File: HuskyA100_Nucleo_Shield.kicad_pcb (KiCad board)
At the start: 2 copper layers, 58.4 x 99.1 mm, 21 parts, among them CN10 HEADER_17x2, CN7 HEADER_10x2, CN8 HEADER_8x2, CN9 HEADER_15x2, J1 Conn_01x03, J2 Conn_01x03, J3 Conn_01x04, J4 Conn_01x04

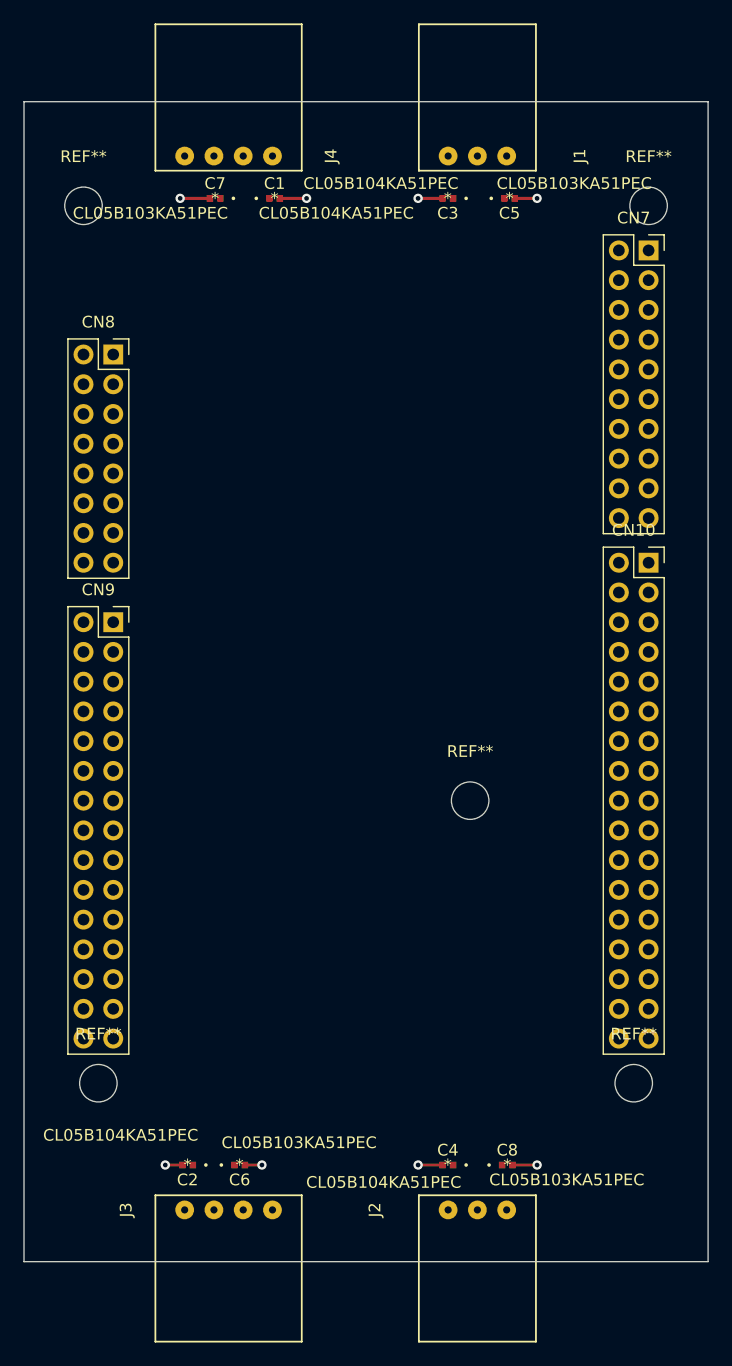
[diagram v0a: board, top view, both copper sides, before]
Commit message: routed the traces
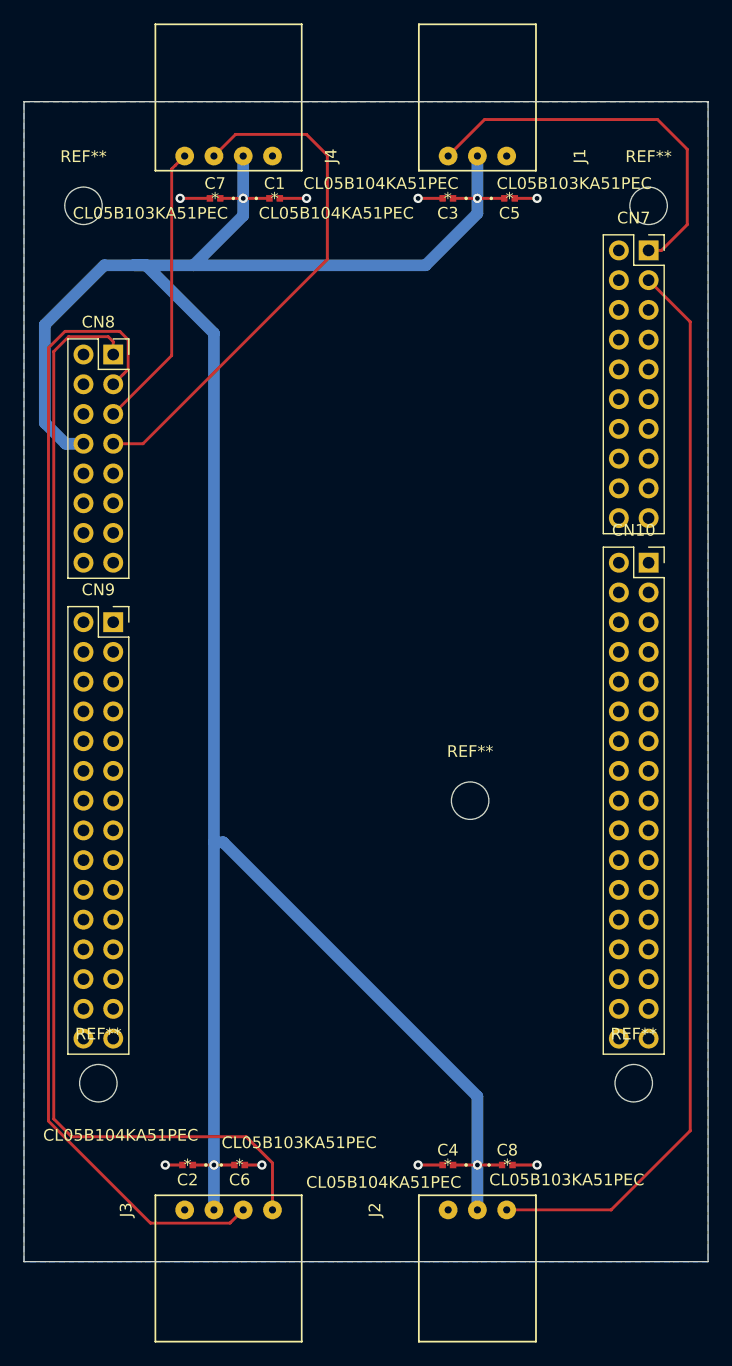
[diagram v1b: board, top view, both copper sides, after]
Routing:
- net 3.3V: track 0.00 -> 210.9 mm, vias 0 -> 4
- net Net-(CN8-Pad3): track 0.00 -> 98.7 mm
- net Net-(CN8-Pad1): track 0.00 -> 96.7 mm
- net Net-(CN7-Pad3): track 0.00 -> 92.6 mm
- net Net-(CN8-Pad7): track 0.00 -> 44.9 mm
- net Net-(CN7-Pad1): track 0.00 -> 33.4 mm
- net Net-(CN8-Pad5): track 0.00 -> 24.6 mm
- added copper zone on B.Cu, net GND
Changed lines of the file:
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@@
     (thickness 1.6)
     (drawings 4)
-    (tracks 16)
+    (tracks 90)
     (zones 0)
     (modules 21)
@@
   (segment (start 125.095 113.665) (end 122.9995 113.665) (width 0.25) (layer F.Cu) (net 7))
   (segment (start 117.0305 113.665) (end 114.935 113.665) (width 0.25) (layer F.Cu) (net 7))
+  (segment (start 135.72 35.56) (end 137.922 33.358) (width 0.25) (layer F.Cu) (net 8))
+  (segment (start 134.62 35.56) (end 135.72 35.56) (width 0.25) (layer F.Cu) (net 8))
+  (segment (start 137.922 33.358) (end 137.922 26.924) (width 0.25) (layer F.Cu) (net 8))
+  (segment (start 137.922 26.924) (end 135.382 24.384) (width 0.25) (layer F.Cu) (net 8))
+  (segment (start 120.616 24.384) (end 117.5 27.5) (width 0.25) (layer F.Cu) (net 8))
+  (segment (start 135.382 24.384) (end 120.616 24.384) (width 0.25) (layer F.Cu) (net 8))
+  (segment (start 138.176 41.656) (end 138.176 110.744) (width 0.25) (layer F.Cu) (net 9))
+  (segment (start 134.62 38.1) (end 138.176 41.656) (width 0.25) (layer F.Cu) (net 9))
+  (segment (start 131.42 117.5) (end 122.5 117.5) (width 0.25) (layer F.Cu) (net 9))
+  (segment (start 138.176 110.744) (end 131.42 117.5) (width 0.25) (layer F.Cu) (net 9))
+  (segment (start 88.9 43.35) (end 88.476 42.926) (width 0.25) (layer F.Cu) (net 26))
+  (segment (start 88.9 44.45) (end 88.9 43.35) (width 0.25) (layer F.Cu) (net 26))
+  (segment (start 88.476 42.926) (end 85.09 42.926) (width 0.25) (layer F.Cu) (net 26))
+  (segment (start 85.09 42.926) (end 83.82 44.196) (width 0.25) (layer F.Cu) (net 26))
+  (segment (start 83.82 44.196) (end 83.82 109.728) (width 0.25) (layer F.Cu) (net 26))
+  (segment (start 83.82 109.728) (end 85.344 111.252) (width 0.25) (layer F.Cu) (net 26))
+  (segment (start 102.5 116.36863) (end 102.5 117.5) (width 0.25) (layer F.Cu) (net 26))
+  (segment (start 100.260002 111.252) (end 102.5 113.491998) (width 0.25) (layer F.Cu) (net 26))
+  (segment (start 102.5 113.491998) (end 102.5 116.36863) (width 0.25) (layer F.Cu) (net 26))
+  (segment (start 85.344 111.252) (end 100.260002 111.252) (width 0.25) (layer F.Cu) (net 26))
+  (segment (start 83.36999 109.9144) (end 83.36999 43.88401) (width 0.25) (layer F.Cu) (net 27))
+  (segment (start 92.080591 118.625001) (end 83.36999 109.9144) (width 0.25) (layer F.Cu) (net 27))
+  (segment (start 98.874999 118.625001) (end 92.080591 118.625001) (width 0.25) (layer F.Cu) (net 27))
+  (segment (start 100 117.5) (end 98.874999 118.625001) (width 0.25) (layer F.Cu) (net 27))
+  (segment (start 84.77801 42.47599) (end 89.46599 42.47599) (width 0.25) (layer F.Cu) (net 27))
+  (segment (start 83.36999 43.88401) (end 84.77801 42.47599) (width 0.25) (layer F.Cu) (net 27))
+  (segment (start 90.17 45.72) (end 89.749999 46.140001) (width 0.25) (layer F.Cu) (net 27))
+  (segment (start 89.749999 46.140001) (end 88.9 46.99) (width 0.25) (layer F.Cu) (net 27))
+  (segment (start 90.17 43.18) (end 90.17 45.72) (width 0.25) (layer F.Cu) (net 27))
+  (segment (start 89.46599 42.47599) (end 90.17 43.18) (width 0.25) (layer F.Cu) (net 27))
+  (segment (start 94.200001 28.299999) (end 95 27.5) (width 0.25) (layer F.Cu) (net 28))
+  (segment (start 93.889999 28.610001) (end 94.200001 28.299999) (width 0.25) (layer F.Cu) (net 28))
+  (segment (start 93.889999 44.540001) (end 93.889999 28.610001) (width 0.25) (layer F.Cu) (net 28))
+  (segment (start 88.9 49.53) (end 93.889999 44.540001) (width 0.25) (layer F.Cu) (net 28))
+  (segment (start 86.36 52.07) (end 84.836 52.07) (width 1) (layer B.Cu) (net 29))
+  (segment (start 84.836 52.07) (end 83.058 50.292) (width 1) (layer B.Cu) (net 29))
+  (segment (start 83.058 50.292) (end 83.058 41.91) (width 1) (layer B.Cu) (net 29))
+  (segment (start 83.058 41.91) (end 88.138 36.83) (width 1) (layer B.Cu) (net 29))
+  (segment (start 100 32.588) (end 100 31.115) (width 1) (layer B.Cu) (net 29))
+  (segment (start 95.758 36.83) (end 100 32.588) (width 1) (layer B.Cu) (net 29))
+  (segment (start 95.758 36.83) (end 115.57 36.83) (width 1) (layer B.Cu) (net 29))
+  (segment (start 120 32.4) (end 120 31.115) (width 1) (layer B.Cu) (net 29))
+  (segment (start 115.57 36.83) (end 120 32.4) (width 1) (layer B.Cu) (net 29))
+  (segment (start 90.678 36.83) (end 91.694 36.83) (width 1) (layer B.Cu) (net 29))
+  (segment (start 88.138 36.83) (end 90.678 36.83) (width 1) (layer B.Cu) (net 29))
+  (segment (start 90.678 36.83) (end 95.758 36.83) (width 1) (layer B.Cu) (net 29))
+  (segment (start 91.694 36.83) (end 97.5 42.636) (width 1) (layer B.Cu) (net 29))
+  (segment (start 97.5 86.106) (end 98.298 86.106) (width 1) (layer B.Cu) (net 29))
+  (segment (start 97.5 42.636) (end 97.5 86.106) (width 1) (layer B.Cu) (net 29))
+  (segment (start 97.5 86.106) (end 97.5 113.665) (width 1) (layer B.Cu) (net 29))
+  (segment (start 120 107.808) (end 120 113.665) (width 1) (layer B.Cu) (net 29))
+  (segment (start 98.298 86.106) (end 120 107.808) (width 1) (layer B.Cu) (net 29))
+  (segment (start 100 31.115) (end 100 27.5) (width 1) (layer B.Cu) (net 29))
+  (via (at 100 31.115) (size 0.8) (drill 0.4) (layers F.Cu B.Cu) (net 29))
+  (segment (start 120 31.115) (end 120 27.5) (width 1) (layer B.Cu) (net 29))
+  (via (at 120 31.115) (size 0.8) (drill 0.4) (layers F.Cu B.Cu) (net 29))
+  (segment (start 97.5 113.665) (end 97.5 117.5) (width 1) (layer B.Cu) (net 29))
+  (via (at 97.5 113.665) (size 0.8) (drill 0.4) (layers F.Cu B.Cu) (net 29))
+  (segment (start 120 113.665) (end 120 117.5) (width 1) (layer B.Cu) (net 29))
+  (via (at 120 113.665) (size 0.8) (drill 0.4) (layers F.Cu B.Cu) (net 29))
+  (segment (start 117.9195 113.665) (end 120 113.665) (width 0.25) (layer F.Cu) (net 29))
+  (segment (start 122.1105 113.665) (end 120 113.665) (width 0.25) (layer F.Cu) (net 29))
+  (segment (start 99.2505 113.665) (end 97.5 113.665) (width 0.25) (layer F.Cu) (net 29))
+  (segment (start 95.6945 113.665) (end 97.5 113.665) (width 0.25) (layer F.Cu) (net 29))
+  (segment (start 98.044 31.115) (end 100 31.115) (width 0.25) (layer F.Cu) (net 29))
+  (segment (start 102.235 31.115) (end 100 31.115) (width 0.25) (layer F.Cu) (net 29))
+  (segment (start 117.9195 31.115) (end 120 31.115) (width 0.25) (layer F.Cu) (net 29))
+  (segment (start 122.301 31.115) (end 120 31.115) (width 0.25) (layer F.Cu) (net 29))
+  (segment (start 88.9 52.07) (end 91.44 52.07) (width 0.25) (layer F.Cu) (net 95))
+  (segment (start 91.44 52.07) (end 107.188 36.322) (width 0.25) (layer F.Cu) (net 95))
+  (segment (start 107.188 36.322) (end 107.188 27.432) (width 0.25) (layer F.Cu) (net 95))
+  (segment (start 107.188 27.432) (end 105.41 25.654) (width 0.25) (layer F.Cu) (net 95))
+  (segment (start 99.346 25.654) (end 97.5 27.5) (width 0.25) (layer F.Cu) (net 95))
+  (segment (start 105.41 25.654) (end 99.346 25.654) (width 0.25) (layer F.Cu) (net 95))
+  (zone (net 7) (net_name GND) (layer B.Cu) (hatch edge 0.508)
+    (connect_pads (clearance 0.508))
+    (min_thickness 0.254)
+    (fill yes (arc_segments 16) (thermal_gap 0.508) (thermal_bridge_width 0.508))
+    (polygon
+      (pts
+        (xy 81.28 22.86) (xy 139.7 22.86) (xy 139.7 121.92) (xy 81.28 121.92)
+      )
+    )
+  )
 )

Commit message: Fixed #3 - replaced bypass caps with 5.6mm x 5.0mm case size to make them more easiy solderable
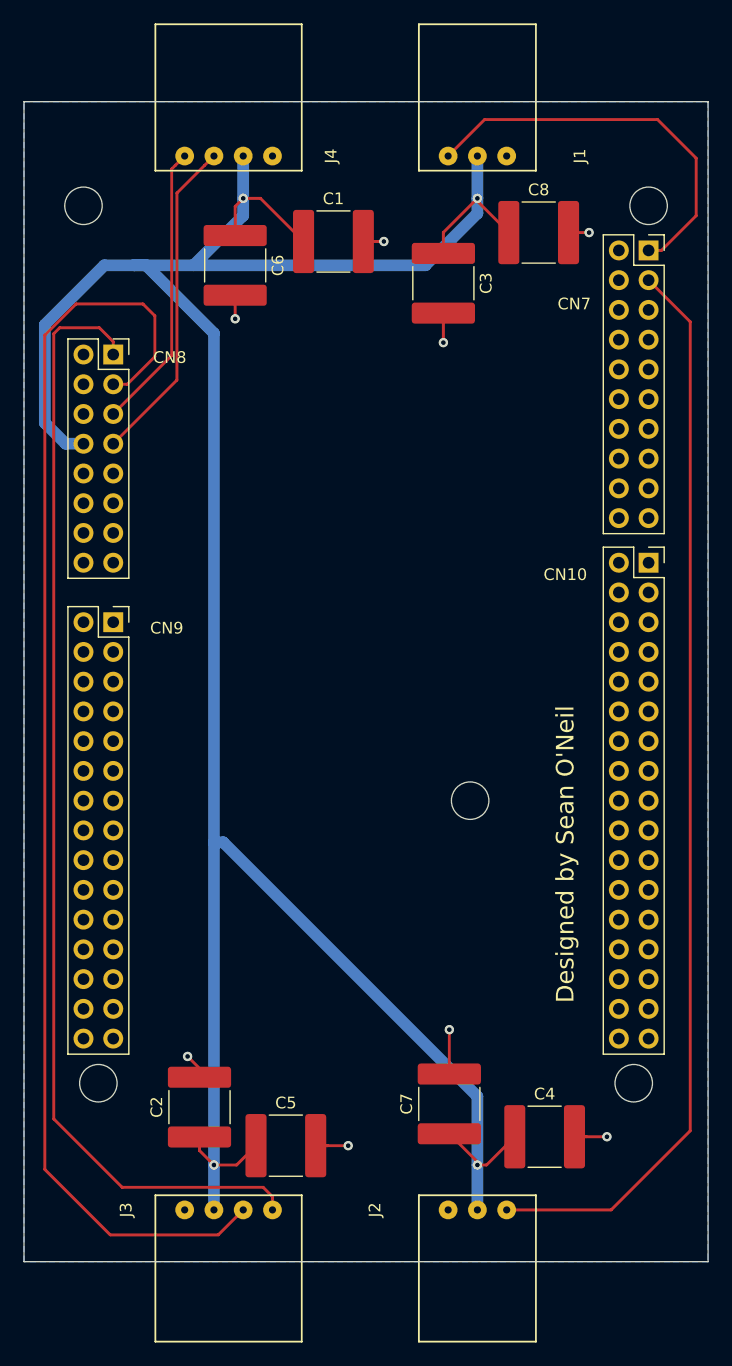
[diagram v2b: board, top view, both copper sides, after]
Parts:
- C1, C2, C3, C4: value CL05B104KA51PEC -> 0.01uF; footprint CL05B104KA51PEC -> Capacitor_SMD:C_2220_5650Metric
- C5, C6, C7, C8: value CL05B103KA51PEC -> 0.1uF; footprint CL05B103KA51PEC -> Capacitor_SMD:C_2220_5650Metric
- moved C5 83.1 mm to (103.6, 112.0)
- moved C7 79.9 mm to (117.6, 108.4), turned to 90 degrees
- moved C8 79.7 mm to (125.2, 34.0)
- moved C6 76.8 mm to (99.3, 36.8), turned to 270 degrees
- moved C4 8.61 mm to (125.7, 111.3), turned to 0 degrees
- moved C3 7.26 mm to (117.1, 38.4), turned to 270 degrees
- moved C1 6.23 mm to (107.7, 34.8)
- moved C2 5.05 mm to (96.3, 108.7), turned to 90 degrees
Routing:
- net 3.3V: track 210.9 -> 229.7 mm
- net Net-(CN8-Pad7): track 44.9 -> 28.1 mm
- net Net-(CN8-Pad3): track 98.7 -> 110.3 mm
- net GND: track 15.9 -> 19.6 mm
- net Net-(CN7-Pad1): track 33.4 -> 34.0 mm
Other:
- board text added: "Designed by Sean O'Neil"

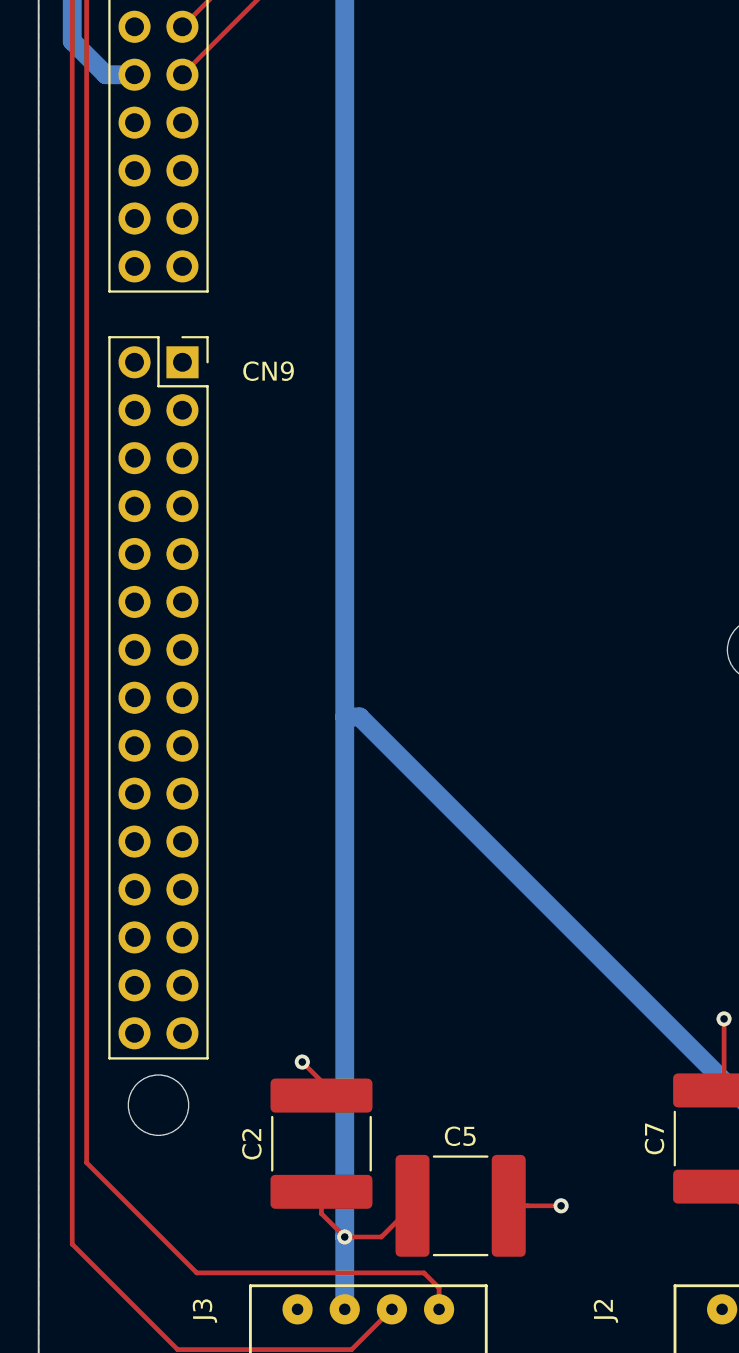
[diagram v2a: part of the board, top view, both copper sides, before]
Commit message: Fix #4 - added power led and authorship. Also made the capacitor pads to 'hand-solderable' for easier assembly
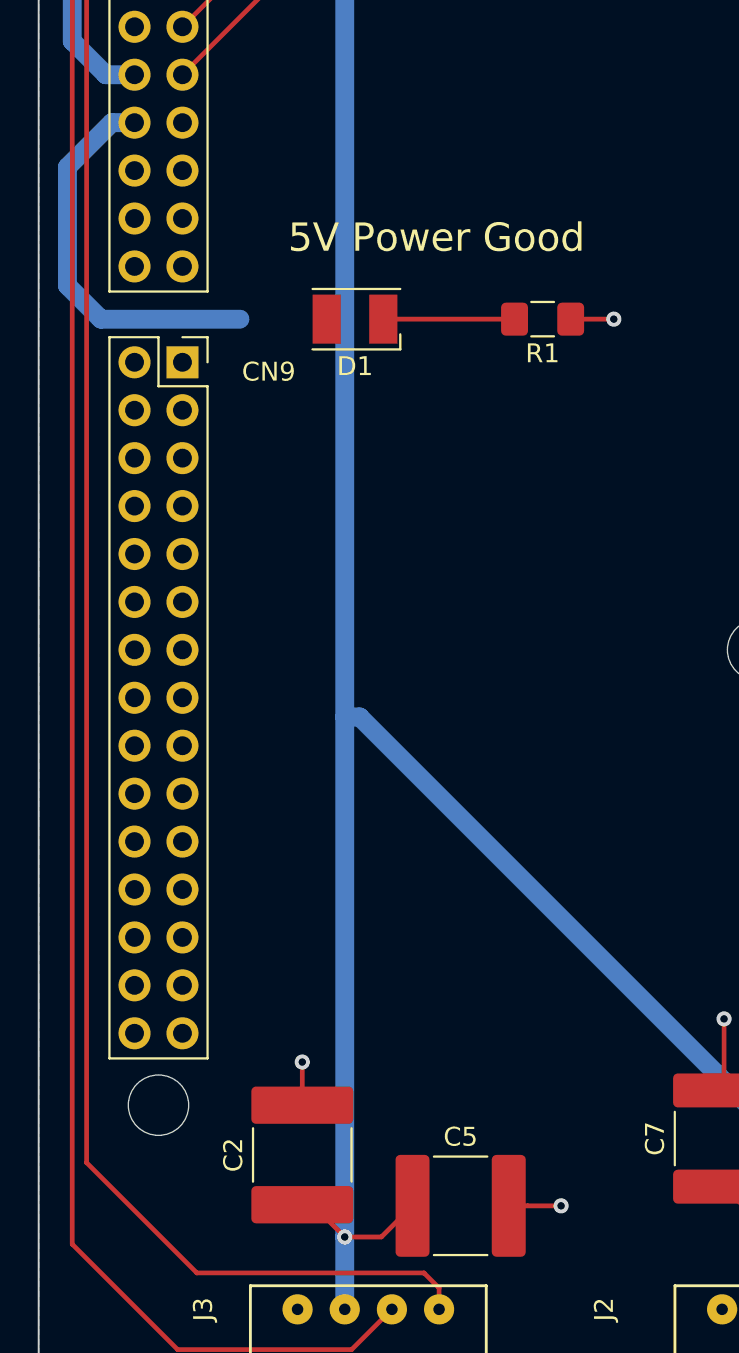
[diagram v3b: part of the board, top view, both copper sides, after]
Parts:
- added D1: LED, LED_SMD:LED_PLCC-2, F.Cu at (98.0, 65.0)
- added R1: 66.5 Ohm, Resistor_SMD:R_1206_3216Metric_Pad1.42x1.75mm_HandSolder, F.Cu at (108.0, 65.0)
- C2: footprint Capacitor_SMD:C_2220_5650Metric -> Capacitor_SMD:C_2220_5650Metric_Pad1.97x5.40mm_HandSolder
- moved C2 1.18 mm to (95.2, 109.3)
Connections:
- CN10 pad 21: Net-(CN10-Pad21) -> GND
- CN10 pad 28: Net-(CN10-Pad28) -> GND
- CN9 pad 11: Net-(CN9-Pad11) -> GND
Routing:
- net 5V: track 0.00 -> 20.7 mm
- net Net-(D1-Pad1): track 0.00 -> 6.95 mm
- net GND: track 19.6 -> 22.0 mm, vias 8 -> 9
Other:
- board text added: "5V Power Good"

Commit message: added a title, miscellaneous fixes changes
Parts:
- moved C6 3.45 mm to (100.3, 40.1)
- moved C2 2.55 mm to (95.0, 106.8)
- moved C1 0.36 mm to (108.0, 35.1)
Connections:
- J1 pad 1: Net-(CN7-Pad1) -> GND
- J1 pad 3: GND -> Net-(CN7-Pad1)
- J2 pad 1: Net-(CN7-Pad3) -> GND
- J2 pad 3: GND -> Net-(CN7-Pad3)
- J3 pad 3: 3.3V -> GND
- J3 pad 4: GND -> 3.3V
- J4 pad 3: 3.3V -> GND
- J4 pad 4: GND -> 3.3V
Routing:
- net 3.3V: track 229.7 -> 249.1 mm
- net Net-(CN7-Pad3): track 92.6 -> 99.8 mm
- net Net-(CN7-Pad1): track 34.0 -> 29.0 mm
- net 5V: track 20.7 -> 25.3 mm, vias 0 -> 1
- net GND: track 22.0 -> 25.7 mm
- net Net-(CN8-Pad7): track 28.1 -> 29.3 mm
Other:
- board text added: "5V Power On"
- board text added: "Wolfgang Motor Controller Shield"
- board text removed: "5V Power Good"
